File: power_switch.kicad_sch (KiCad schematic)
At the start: 16 parts, among them J4 Power Output, U3 BTS7004-1EPP

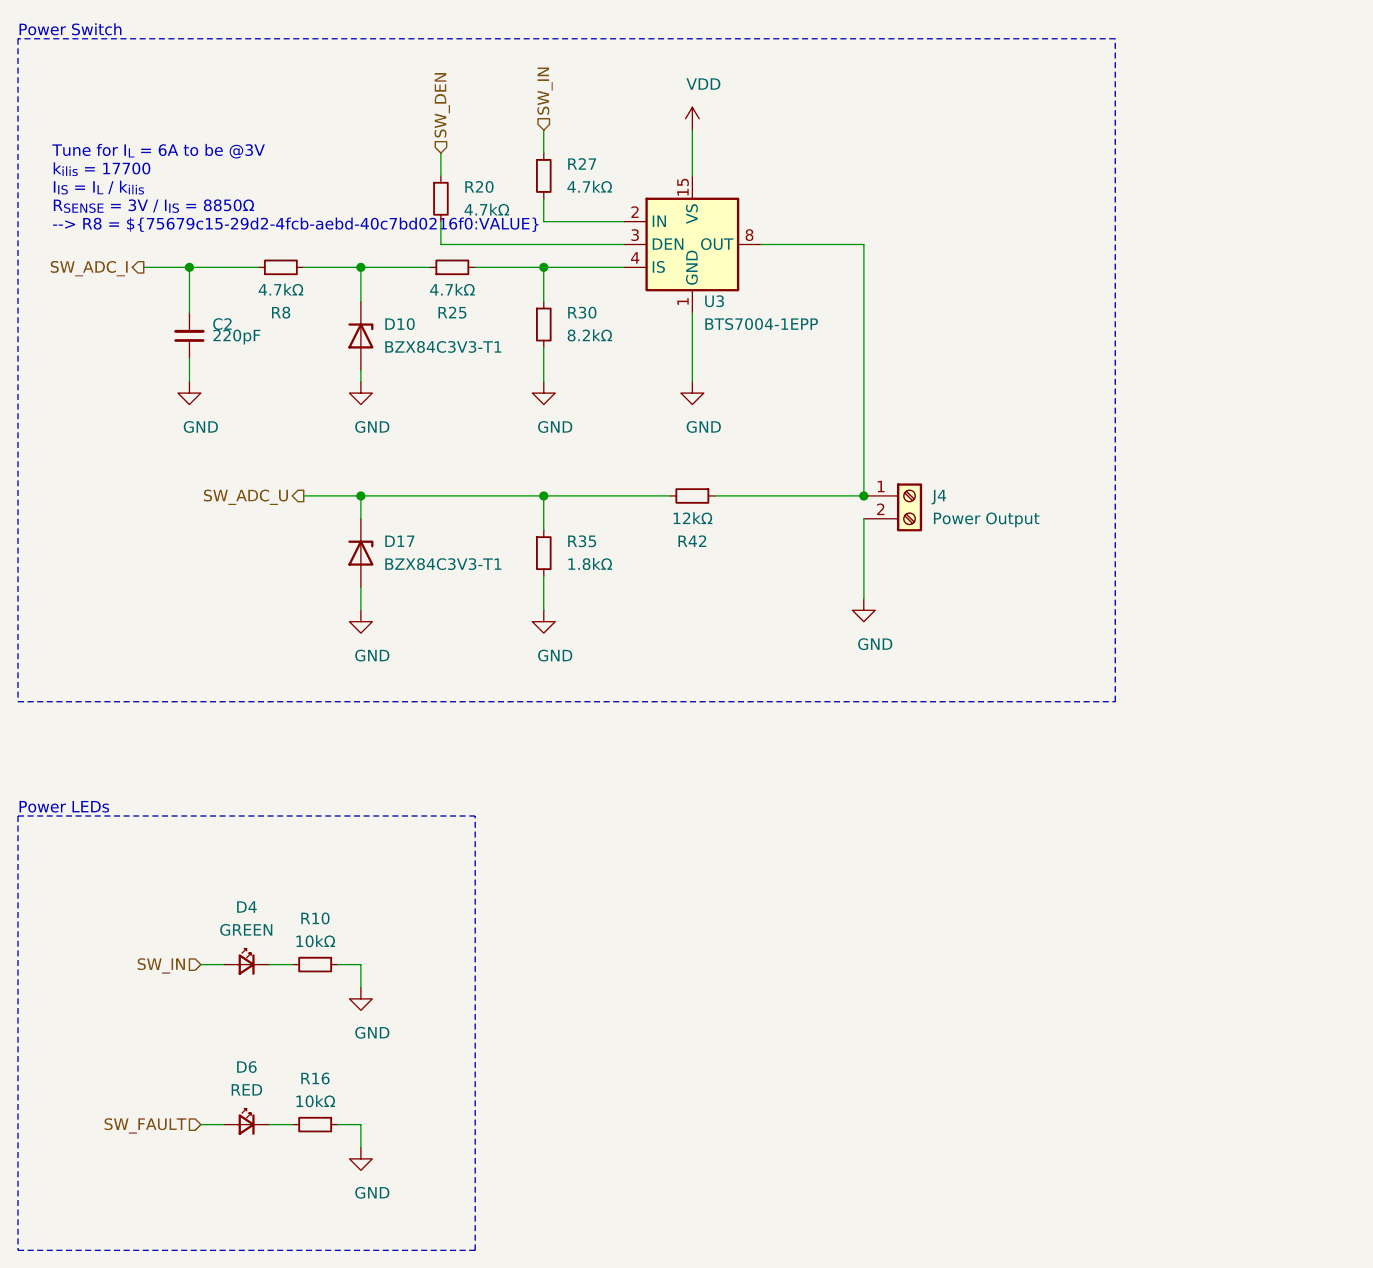
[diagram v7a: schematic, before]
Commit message: updated footprints, adjustments in placement
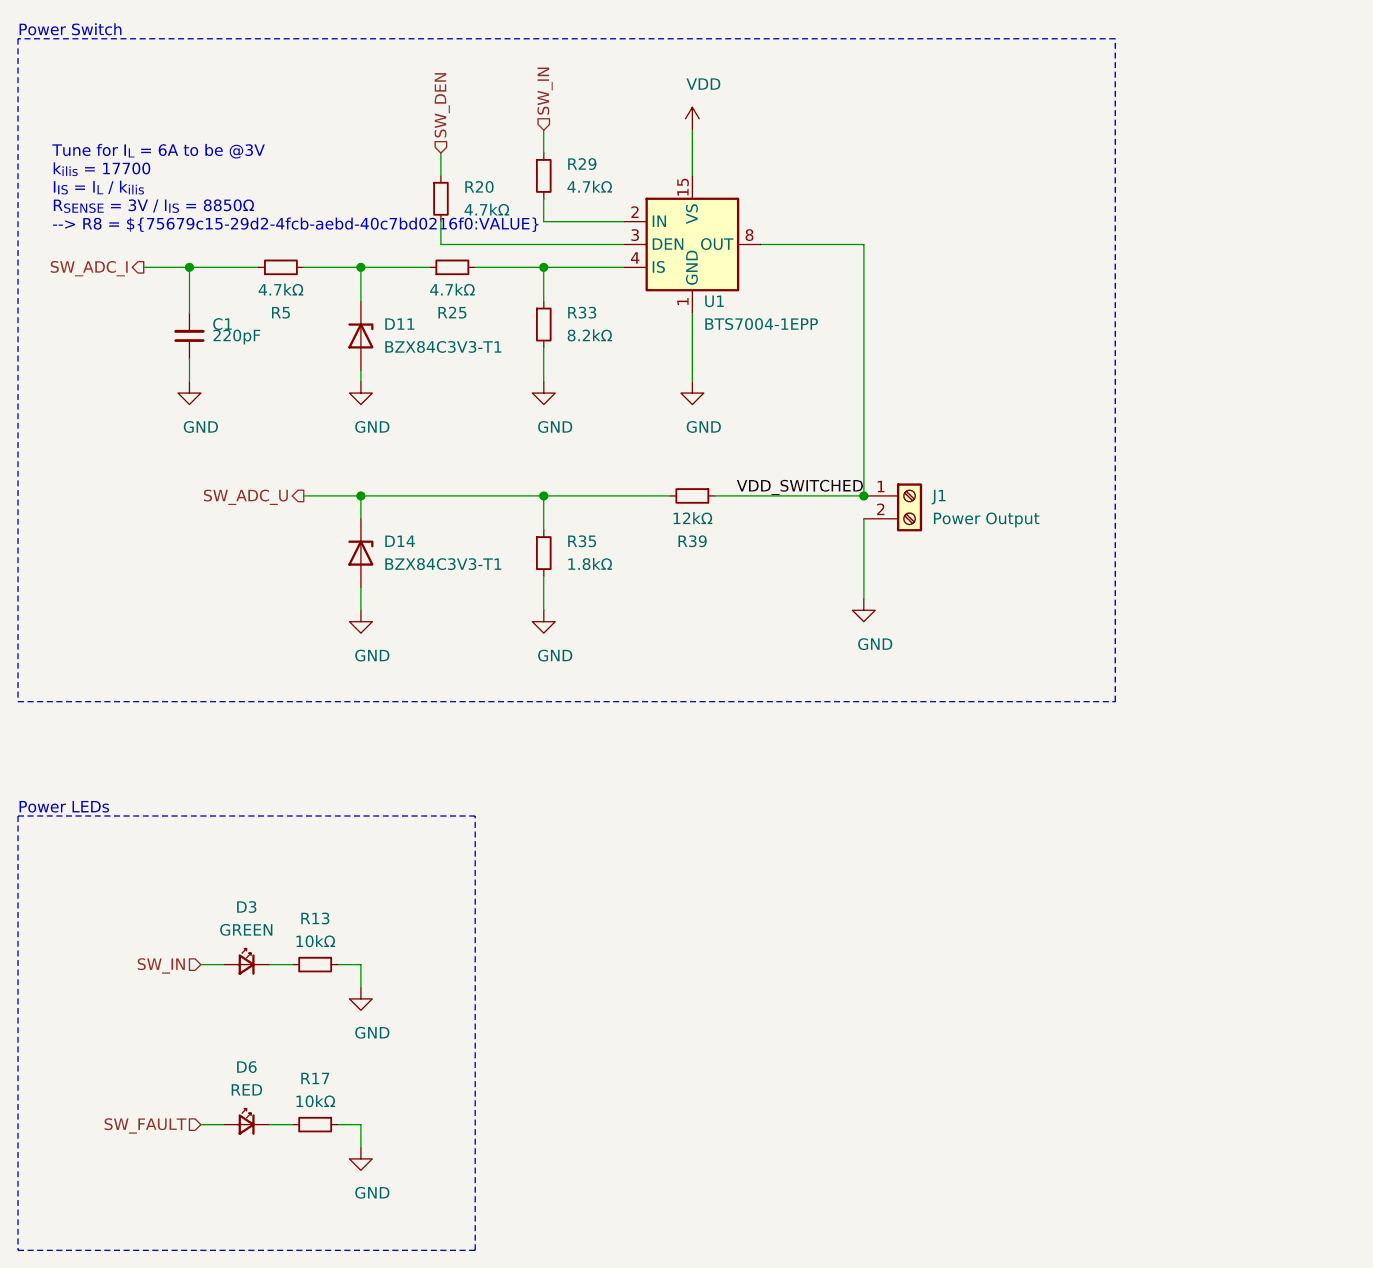
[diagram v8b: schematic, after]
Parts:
- J1: renamed from J4; footprint TerminalBlock_RND:TerminalBlock_RND_205-00287_1x02_P5.08mm_Horizontal -> TerminalBlock_RND:TerminalBlock_RND_205-00045_1x02_P5.00mm_Horizontal
- renumbered C2 to C1, D10 to D11, D17 to D14, D4 to D3, R10 to R13, R16 to R17, R27 to R29, R30 to R33, R42 to R39, R8 to R5, U3 to U1
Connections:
- net VDD_SWITCHED: now reaches J1.1 (Pin_1), R39.1, U1.10 (OUT), U1.12 (OUT), U1.13 (OUT), U1.14 (OUT), U1.8 (OUT), U1.9 (OUT)
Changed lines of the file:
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@@
     (effects (font (size 1.27 1.27)) (justify left bottom))
+  )
+  (label "VDD_SWITCHED" (at 113.03 69.85 180)
+    (effects (font (size 1.27 1.27)) (justify right bottom))
   )
   (hierarchical_label "SW_ADC_I" (shape output) (at 33.02 44.45 180)
@@
   (symbol (lib_id "power:GND") (at 57.15 57.15 0)
     (in_bom yes) (on_board yes)
-    (property "Reference" "#PWR019" (id 0) (at 57.15 63.5 0)
+    (property "Reference" "#PWR021" (id 0) (at 57.15 63.5 0)
       (effects (font (size 1.27 1.27)) hide)
     )
@@
   (symbol (lib_id "power:GND") (at 57.15 124.46 0)
     (in_bom yes) (on_board yes)
-    (property "Reference" "#PWR026" (id 0) (at 57.15 130.81 0)
+    (property "Reference" "#PWR028" (id 0) (at 57.15 130.81 0)
       (effects (font (size 1.27 1.27)) hide)
     )
@@
   (symbol (lib_id "power:GND") (at 57.15 142.24 0)
     (in_bom yes) (on_board yes)
-    (property "Reference" "#PWR033" (id 0) (at 57.15 148.59 0)
+    (property "Reference" "#PWR032" (id 0) (at 57.15 148.59 0)
       (effects (font (size 1.27 1.27)) hide)
     )
@@
   (symbol (lib_id "power:GND") (at 77.47 57.15 0)
     (in_bom yes) (on_board yes)
-    (property "Reference" "#PWR037" (id 0) (at 77.47 63.5 0)
+    (property "Reference" "#PWR038" (id 0) (at 77.47 63.5 0)
       (effects (font (size 1.27 1.27)) hide)
     )
@@
   (symbol (lib_id "power:GND") (at 77.47 82.55 0)
     (in_bom yes) (on_board yes)
-    (property "Reference" "#PWR040" (id 0) (at 77.47 88.9 0)
+    (property "Reference" "#PWR041" (id 0) (at 77.47 88.9 0)
       (effects (font (size 1.27 1.27)) hide)
     )
@@
   (symbol (lib_id "power:GND") (at 93.98 57.15 0)
     (in_bom yes) (on_board yes)
-    (property "Reference" "#PWR051" (id 0) (at 93.98 63.5 0)
+    (property "Reference" "#PWR049" (id 0) (at 93.98 63.5 0)
       (effects (font (size 1.27 1.27)) hide)
     )
@@
   (symbol (lib_id "Device:R_Small") (at 48.26 44.45 90)
     (in_bom yes) (on_board yes)
-    (property "Reference" "R8" (id 0) (at 48.26 49.53 90))
+    (property "Reference" "R5" (id 0) (at 48.26 49.53 90))
     (property "Value" "4.7kΩ" (id 1) (at 48.26 46.99 90))
     (property "Footprint" "Resistor_SMD:R_0603_1608Metric" (id 2) (at 48.26 46.228 90)
@@
   (symbol (lib_id "Device:R_Small") (at 52.07 121.92 270)
     (in_bom yes) (on_board yes)
-    (property "Reference" "R10" (id 0) (at 52.07 116.84 90))
+    (property "Reference" "R13" (id 0) (at 52.07 116.84 90))
     (property "Value" "10kΩ" (id 1) (at 52.07 119.38 90))
     (property "Footprint" "Resistor_SMD:R_0603_1608Metric" (id 2) (at 52.07 120.142 90)
@@
   (symbol (lib_id "Device:R_Small") (at 52.07 139.7 270)
     (in_bom yes) (on_board yes)
-    (property "Reference" "R16" (id 0) (at 52.07 134.62 90))
+    (property "Reference" "R17" (id 0) (at 52.07 134.62 90))
     (property "Value" "10kΩ" (id 1) (at 52.07 137.16 90))
     (property "Footprint" "Resistor_SMD:R_0603_1608Metric" (id 2) (at 52.07 137.922 90)
@@
   (symbol (lib_id "Device:R_Small") (at 77.47 34.29 0)
     (in_bom yes) (on_board yes)
-    (property "Reference" "R27" (id 0) (at 80.01 33.02 0)
+    (property "Reference" "R29" (id 0) (at 80.01 33.02 0)
       (effects (font (size 1.27 1.27)) (justify left))
     )
@@
   (symbol (lib_id "Device:R_Small") (at 77.47 50.8 0)
     (in_bom yes) (on_board yes)
-    (property "Reference" "R30" (id 0) (at 80.01 49.53 0)
+    (property "Reference" "R33" (id 0) (at 80.01 49.53 0)
       (effects (font (size 1.27 1.27)) (justify left))
     )
@@
   (symbol (lib_id "Device:R_Small") (at 93.98 69.85 270)
     (in_bom yes) (on_board yes)
-    (property "Reference" "R42" (id 0) (at 93.98 74.93 90))
+    (property "Reference" "R39" (id 0) (at 93.98 74.93 90))
     (property "Value" "12kΩ" (id 1) (at 93.98 72.39 90))
     (property "Footprint" "Resistor_SMD:R_0603_1608Metric" (id 2) (at 93.98 69.85 0)
@@
   (symbol (lib_id "Device:LED_Small") (at 44.45 121.92 0) (mirror y)
     (in_bom yes) (on_board yes)
-    (property "Reference" "D4" (id 0) (at 44.45 115.57 0))
+    (property "Reference" "D3" (id 0) (at 44.45 115.57 0))
     (property "Value" "GREEN" (id 1) (at 44.45 118.11 0))
     (property "Footprint" "LED_SMD:LED_0603_1608Metric" (id 2) (at 44.45 121.92 90)
@@
   (symbol (lib_id "Device:C_Small") (at 38.1 52.07 180)
     (in_bom yes) (on_board yes)
-    (property "Reference" "C2" (id 0) (at 40.64 50.8 0)
+    (property "Reference" "C1" (id 0) (at 40.64 50.8 0)
       (effects (font (size 1.27 1.27)) (justify right))
     )
@@
   (symbol (lib_id "Diode:DZ2S033X0L") (at 57.15 52.07 270)
     (in_bom yes) (on_board yes)
-    (property "Reference" "D10" (id 0) (at 59.69 50.8 90)
+    (property "Reference" "D11" (id 0) (at 59.69 50.8 90)
       (effects (font (size 1.27 1.27)) (justify left))
     )
@@
   (symbol (lib_id "Diode:DZ2S033X0L") (at 57.15 76.2 270)
     (in_bom yes) (on_board yes)
-    (property "Reference" "D17" (id 0) (at 59.69 74.93 90)
+    (property "Reference" "D14" (id 0) (at 59.69 74.93 90)
       (effects (font (size 1.27 1.27)) (justify left))
     )
@@
   (symbol (lib_id "Connector:Screw_Terminal_01x02") (at 118.11 69.85 0)
     (in_bom yes) (on_board yes)
-    (property "Reference" "J4" (id 0) (at 120.65 69.85 0)
+    (property "Reference" "J1" (id 0) (at 120.65 69.85 0)
       (effects (font (size 1.27 1.27)) (justify left))
     )
@@
       (effects (font (size 1.27 1.27)) (justify left))
     )
-    (property "Footprint" "TerminalBlock_RND:TerminalBlock_RND_205-00287_1x02_P5.08mm_Horizontal" (id 2) (at 118.11 69.85 0)
+    (property "Footprint" "TerminalBlock_RND:TerminalBlock_RND_205-00045_1x02_P5.00mm_Horizontal" (id 2) (at 118.11 69.85 0)
       (effects (font (size 1.27 1.27)) hide)
     )
@@
   (symbol (lib_id "Power_Management:BTS7004-1EPP") (at 93.98 41.91 0)
     (in_bom yes) (on_board yes)
-    (property "Reference" "U3" (id 0) (at 95.25 48.26 0)
-      (effects (font (size 1.27 1.27)) (justify left))
-    )
+    (property "Reference" "U1" (id 0) (at 95.25 48.26 0)
+      (effects (font (size 1.27 1.27)) (justify left))
+    )
